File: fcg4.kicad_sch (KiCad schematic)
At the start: 0 parts

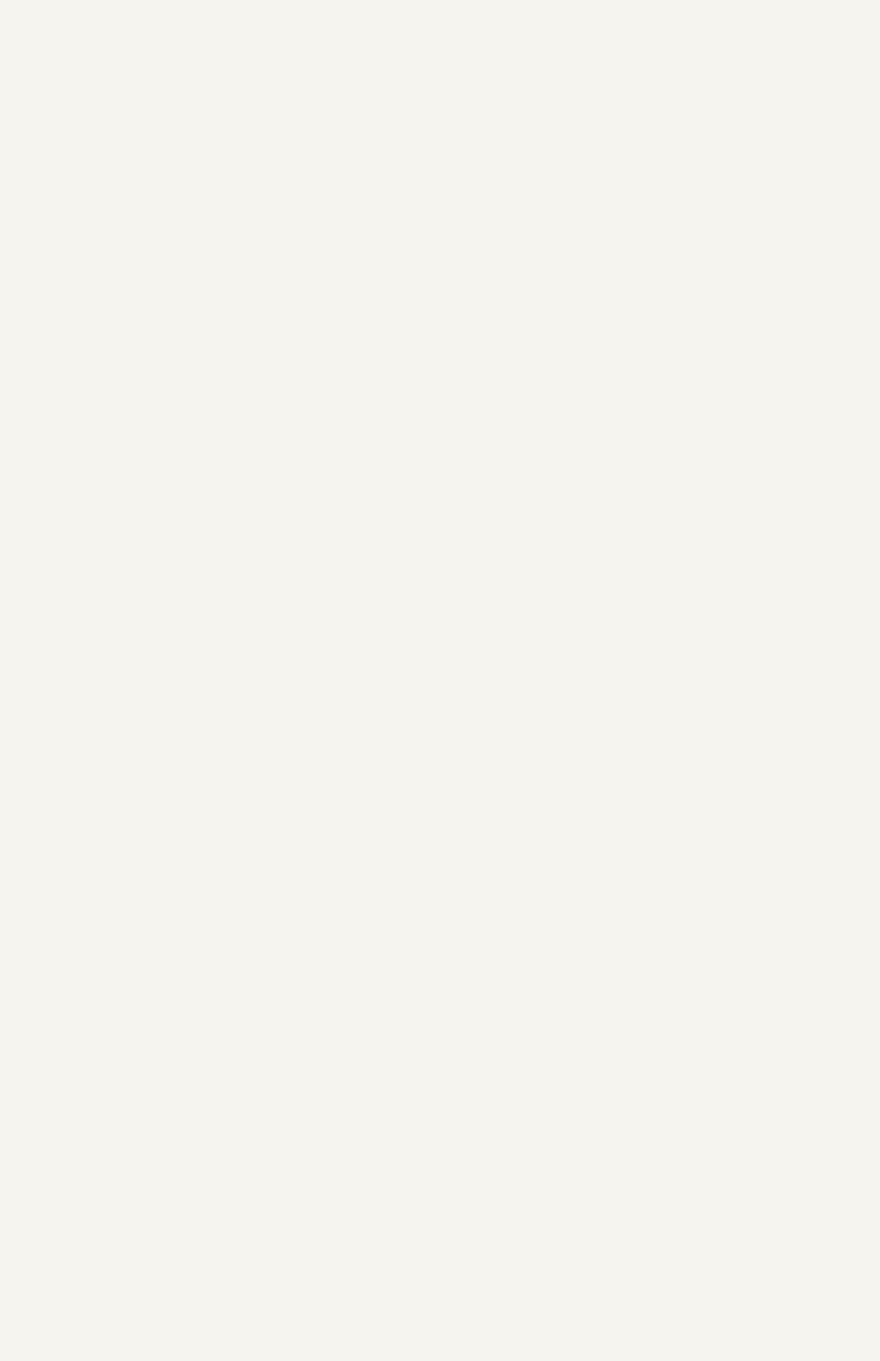
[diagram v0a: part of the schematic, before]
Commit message: first components on schematic and few wiring
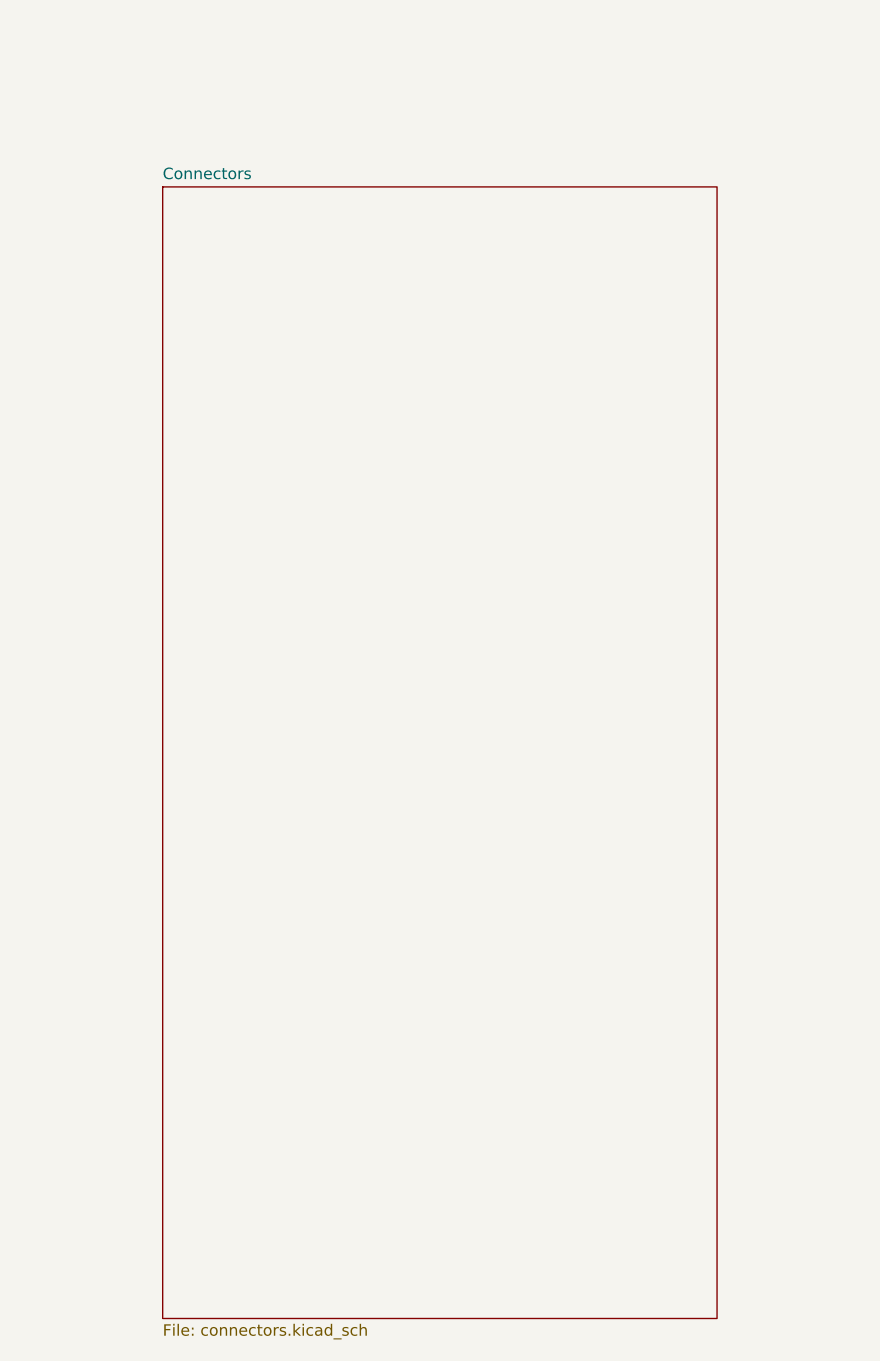
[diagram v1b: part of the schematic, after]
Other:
- added sheet Connectors (connectors.kicad_sch)
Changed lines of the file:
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@@
+	)
+	(sheet
+		(at -44.45 302.26)
+		(size 61.595 125.73)
+		(exclude_from_sim no)
+		(in_bom yes)
+		(on_board yes)
+		(dnp no)
+		(fields_autoplaced yes)
+		(stroke
+			(width 0.1524)
+			(type solid)
+		)
+		(fill
+			(color 0 0 0 0.0000)
+		)
+		(property "Sheetname" "Connectors"
+			(at -44.45 301.5484 0)
+			(effects
+				(font
+					(size 1.27 1.27)
+				)
+				(justify left bottom)
+			)
+		)
+		(property "Sheetfile" "connectors.kicad_sch"
+			(at -44.45 428.5746 0)
+			(effects
+				(font
+					(size 1.27 1.27)
+				)
+				(justify left top)
+			)
+		)
+		(instances
+			(project "fcg4"
+				(path "/ebe93c2f-0aae-4f69-99fc-930f63b0ac94"
+					(page "5")
+				)
+			)
+		)
 	)
 	(sheet

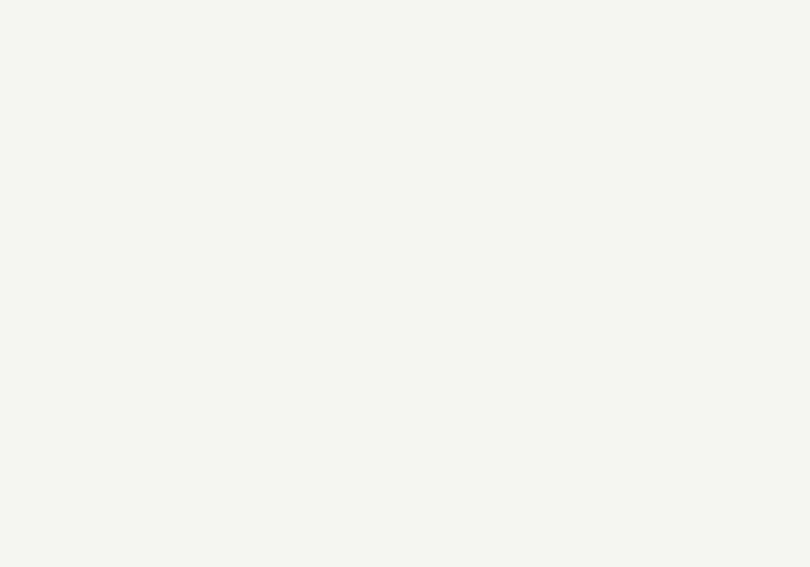
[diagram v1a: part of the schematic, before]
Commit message: - Removed SBUS receiver support in uart1 and added esc telemetry in uart2 - Added a new Mounting Hole symbol with properties and graphical representation in the schematic (fcg4.kicad_sch). (MountingHoles_30.5x30.5mm_Standard.kicad_mod) with appropriate pads and attributes. - Started PCB editor
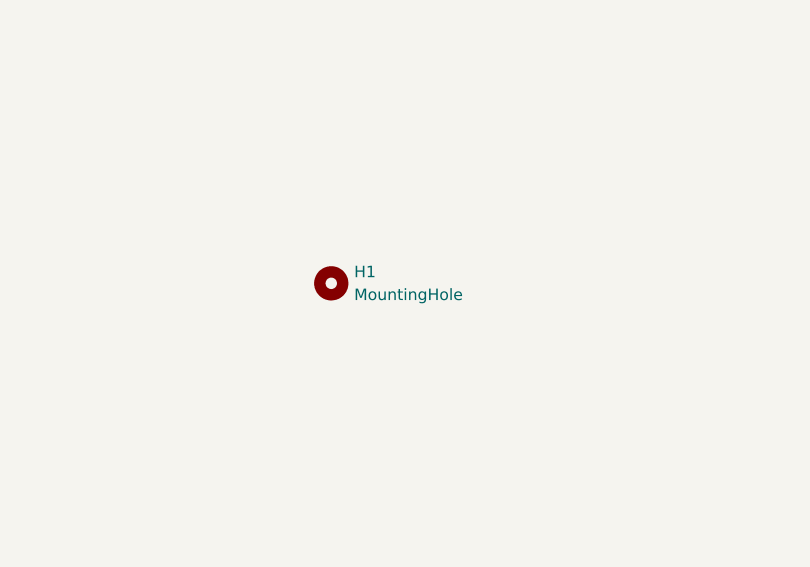
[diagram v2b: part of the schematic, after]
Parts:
- added H1: MountingHole, fcg4_fp:MountingHoles_30.5x30.5mm_Standard, symbol fcg4:MountingHole
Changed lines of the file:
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@@
 	(generator_version "9.0")
 	(paper "A4")
+	(symbol
+		(lib_id "fcg4:MountingHole")
+		(at 125.73 60.96 0)
+		(unit 1)
+		(exclude_from_sim no)
+		(in_bom no)
+		(on_board yes)
+		(dnp no)
+		(fields_autoplaced yes)
+		(property "Reference" "H1"
+			(at 128.27 59.6899 0)
+			(effects
+				(font
+					(size 1.27 1.27)
+				)
+				(justify left)
+			)
+		)
+		(property "Value" "MountingHole"
+			(at 128.27 62.2299 0)
+			(effects
+				(font
+					(size 1.27 1.27)
+				)
+				(justify left)
+			)
+		)
+		(property "Footprint" "fcg4_fp:MountingHoles_30.5x30.5mm_Standard"
+			(at 126.492 68.072 0)
+			(effects
+				(font
+					(size 1.27 1.27)
+				)
+				(hide yes)
+			)
+		)
+		(property "Datasheet" "~"
+			(at 125.73 60.96 0)
+			(effects
+				(font
+					(size 1.27 1.27)
+				)
+				(hide yes)
+			)
+		)
+		(property "Description" "Mounting Hole without connection"
+			(at 125.476 65.786 0)
+			(effects
+				(font
+					(size 1.27 1.27)
+				)
+				(hide yes)
+			)
+		)
+		(instances
+			(project ""
+				(path "/ebe93c2f-0aae-4f69-99fc-930f63b0ac94"
+					(reference "H1")
+					(unit 1)
+				)
+			)
+		)
+	)
 	(sheet
 		(at -182.88 7.62)
